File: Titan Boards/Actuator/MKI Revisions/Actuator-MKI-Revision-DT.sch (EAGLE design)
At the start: 104 parts, among them Q1 MOSFET-NCH-AO3404A, Q10 MOSFET-NCH-AO3404A, Q11 MOSFET-NCH-AO3404A, Q12 MOSFET-NCH-AO3404A, Q13 MOSFET-NCH-AO3404A, Q14 MOSFET-NCH-AO3404A, Q15 MOSFET-NCH-AO3404A, Q16 MOSFET-NCH-AO3404A, Q17 MOSFET-NCH-AO3404A, Q18 FDD4141TO252, Q2 MOSFET-NCH-AO3404A, Q3 MOSFET-NCH-AO3404A, Q4 MOSFET-NCH-AO3404A, Q5 MOSFET-NCH-AO3404A, Q6 FDD4141TO252, Q7 MOSFET-NCH-AO3404A, Q8 MOSFET-NCH-AO3404A, Q9 MOSFET-NCH-AO3404A, U1 DRV8816PWPR, U2 W25Q128BVEIG, Y2 16MHz

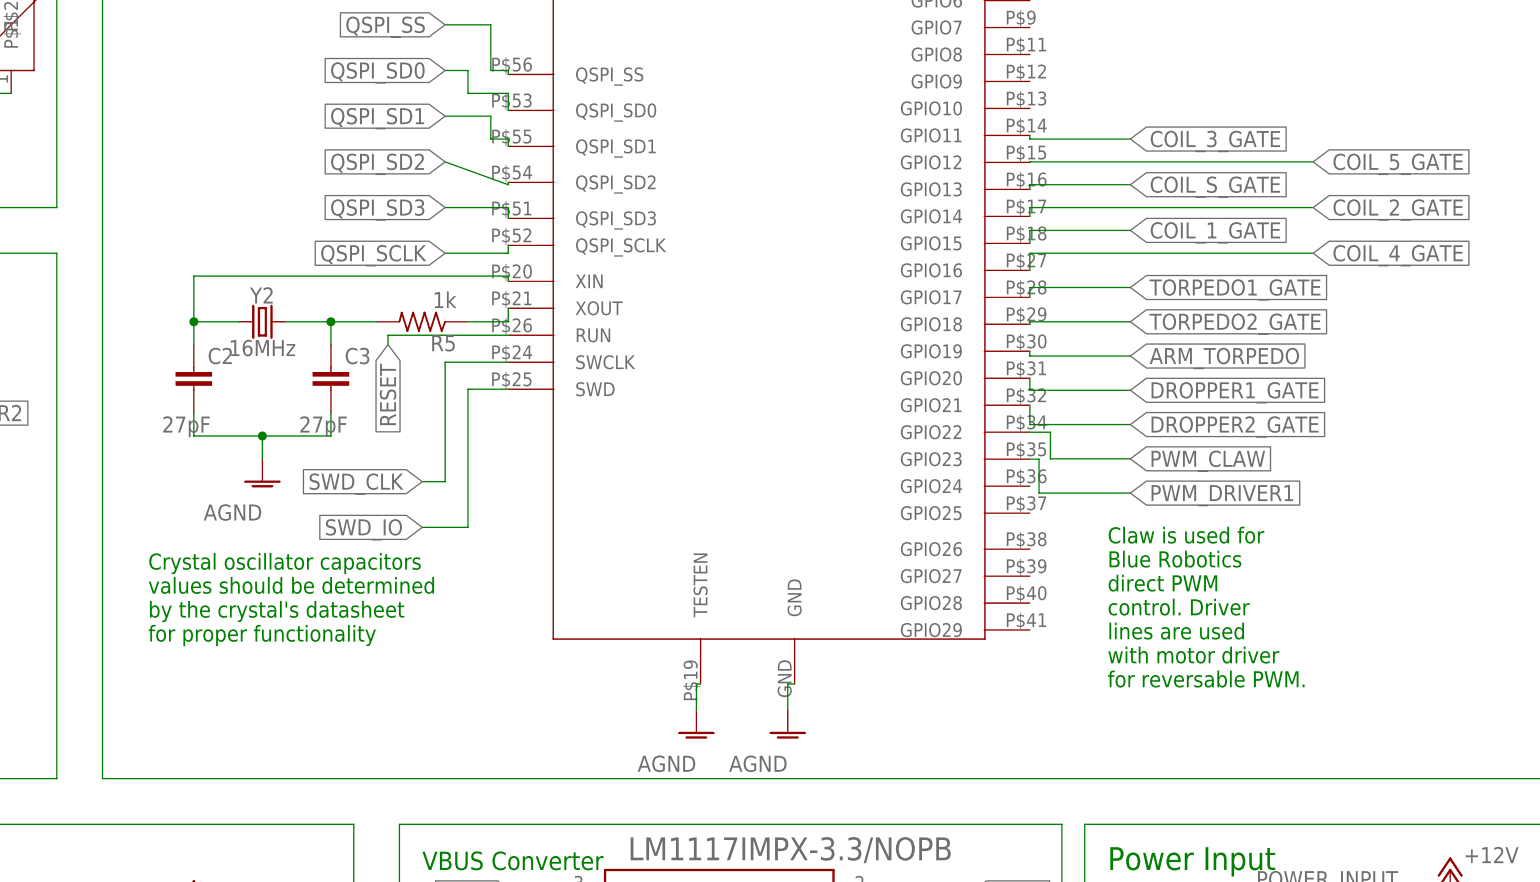
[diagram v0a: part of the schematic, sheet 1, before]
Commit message: Corrected some wiring and moved name tags
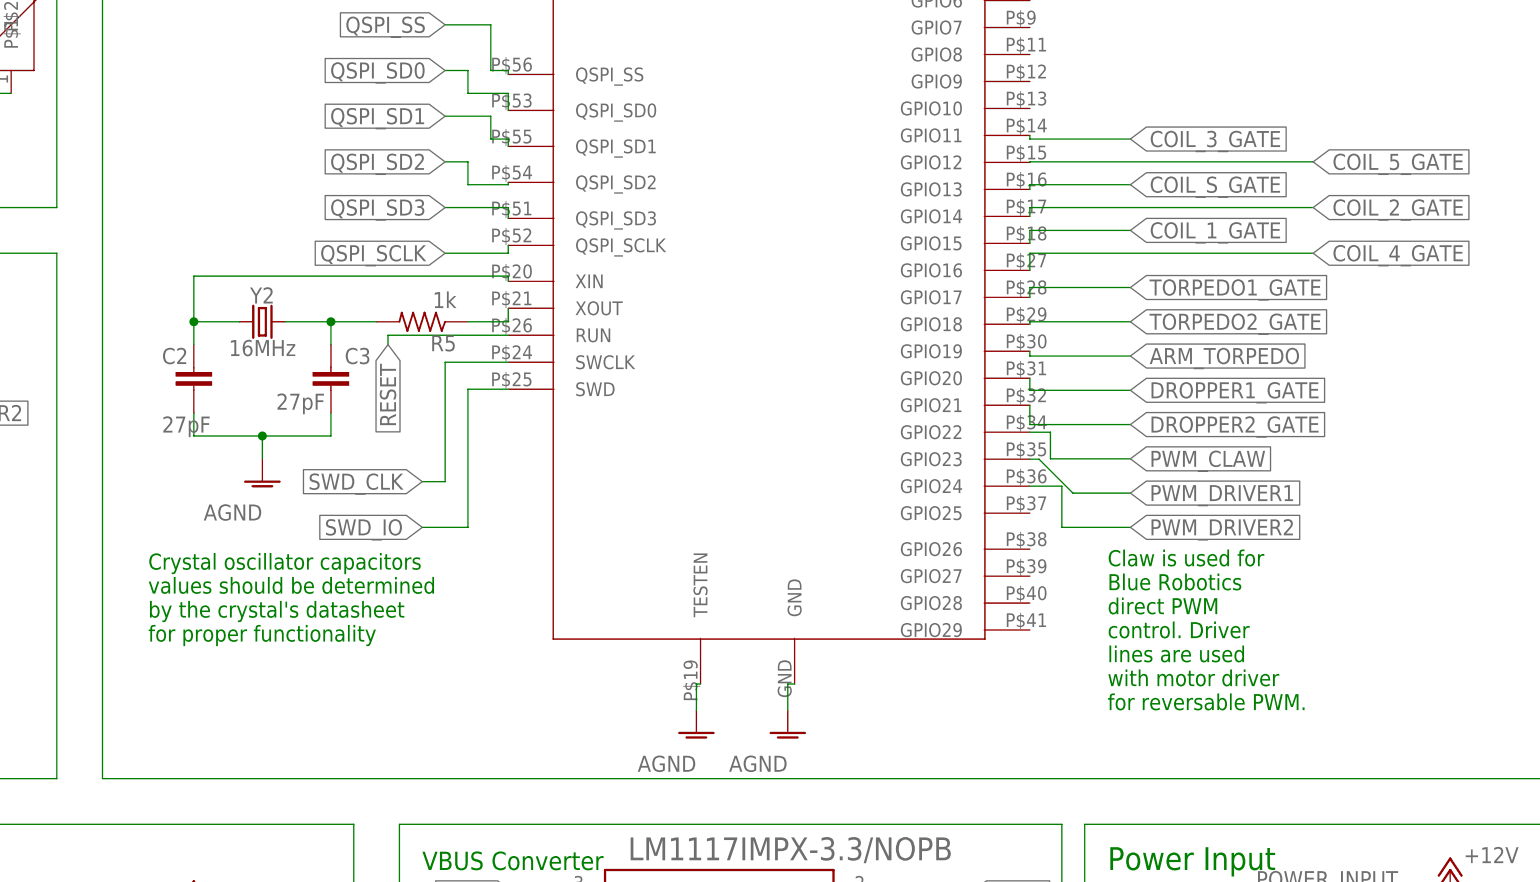
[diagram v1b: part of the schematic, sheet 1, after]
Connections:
- net PWM_DRIVER2: now also U$9.GPIO24
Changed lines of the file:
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@@
 <text x="251.46" y="45.72" size="2.032" layer="91">VBUS Converter</text>
 <text x="274.066" y="246.38" size="2.54" layer="91">PMIC Motor Driver</text>
-<text x="327.66" y="66.04" size="1.778" layer="91">Claw is used for
+<text x="327.66" y="63.5" size="1.778" layer="91">Claw is used for
 Blue Robotics
 direct PWM
@@
 </instance>
 <instance part="C2" gate="G$1" x="226.06" y="101.6" smashed="yes">
-<attribute name="NAME" x="227.584" y="101.981" size="1.778" layer="95"/>
+<attribute name="NAME" x="222.504" y="101.981" size="1.778" layer="95"/>
 <attribute name="VALUE" x="222.504" y="94.361" size="1.778" layer="96"/>
 </instance>
 <instance part="C3" gate="G$1" x="241.3" y="101.6" smashed="yes">
 <attribute name="NAME" x="242.824" y="101.981" size="1.778" layer="95"/>
-<attribute name="VALUE" x="237.744" y="94.361" size="1.778" layer="96"/>
+<attribute name="VALUE" x="235.204" y="96.901" size="1.778" layer="96"/>
 </instance>
 <instance part="AGND3" gate="VR1" x="233.68" y="88.9" smashed="yes">
@@
 <segment>
 <label x="330.2" y="87.63" size="1.778" layer="95" xref="yes"/>
-<wire x1="330.2" y1="87.63" x2="320.04" y2="87.63" width="0.1524" layer="91"/>
-<wire x1="320.04" y1="87.63" x2="320.04" y2="91.4" width="0.1524" layer="91"/>
+<wire x1="330.2" y1="87.63" x2="323.81" y2="87.63" width="0.1524" layer="91"/>
+<wire x1="323.81" y1="87.63" x2="320.04" y2="91.4" width="0.1524" layer="91"/>
 <pinref part="U$9" gate="G$1" pin="GPIO23"/>
 <wire x1="320.04" y1="91.4" x2="319.02" y2="91.4" width="0.1524" layer="91"/>
@@
 <wire x1="285.242" y1="226.06" x2="277.622" y2="226.06" width="0.1524" layer="91"/>
 <label x="277.622" y="226.06" size="1.524" layer="95" rot="R270" xref="yes"/>
+</segment>
+<segment>
+<pinref part="U$9" gate="G$1" pin="GPIO24"/>
+<wire x1="319.02" y1="88.4" x2="322.58" y2="88.4" width="0.1524" layer="91"/>
+<wire x1="322.58" y1="88.4" x2="322.58" y2="83.82" width="0.1524" layer="91"/>
+<wire x1="322.58" y1="83.82" x2="330.2" y2="83.82" width="0.1524" layer="91"/>
+<label x="330.2" y="83.82" size="1.778" layer="95" xref="yes"/>
 </segment>
 </net>
@@
 <pinref part="U$9" gate="G$1" pin="QSPI_SD2"/>
 <wire x1="261.02" y1="122.18" x2="261.02" y2="121.92" width="0.1524" layer="91"/>
-<wire x1="261.02" y1="121.92" x2="254" y2="124.46" width="0.1524" layer="91"/>
+<wire x1="261.02" y1="121.92" x2="256.54" y2="121.92" width="0.1524" layer="91"/>
+<wire x1="256.54" y1="121.92" x2="256.54" y2="124.46" width="0.1524" layer="91"/>
+<wire x1="256.54" y1="124.46" x2="254" y2="124.46" width="0.1524" layer="91"/>
 <label x="254" y="124.46" size="1.778" layer="95" rot="R180" xref="yes"/>
 </segment>

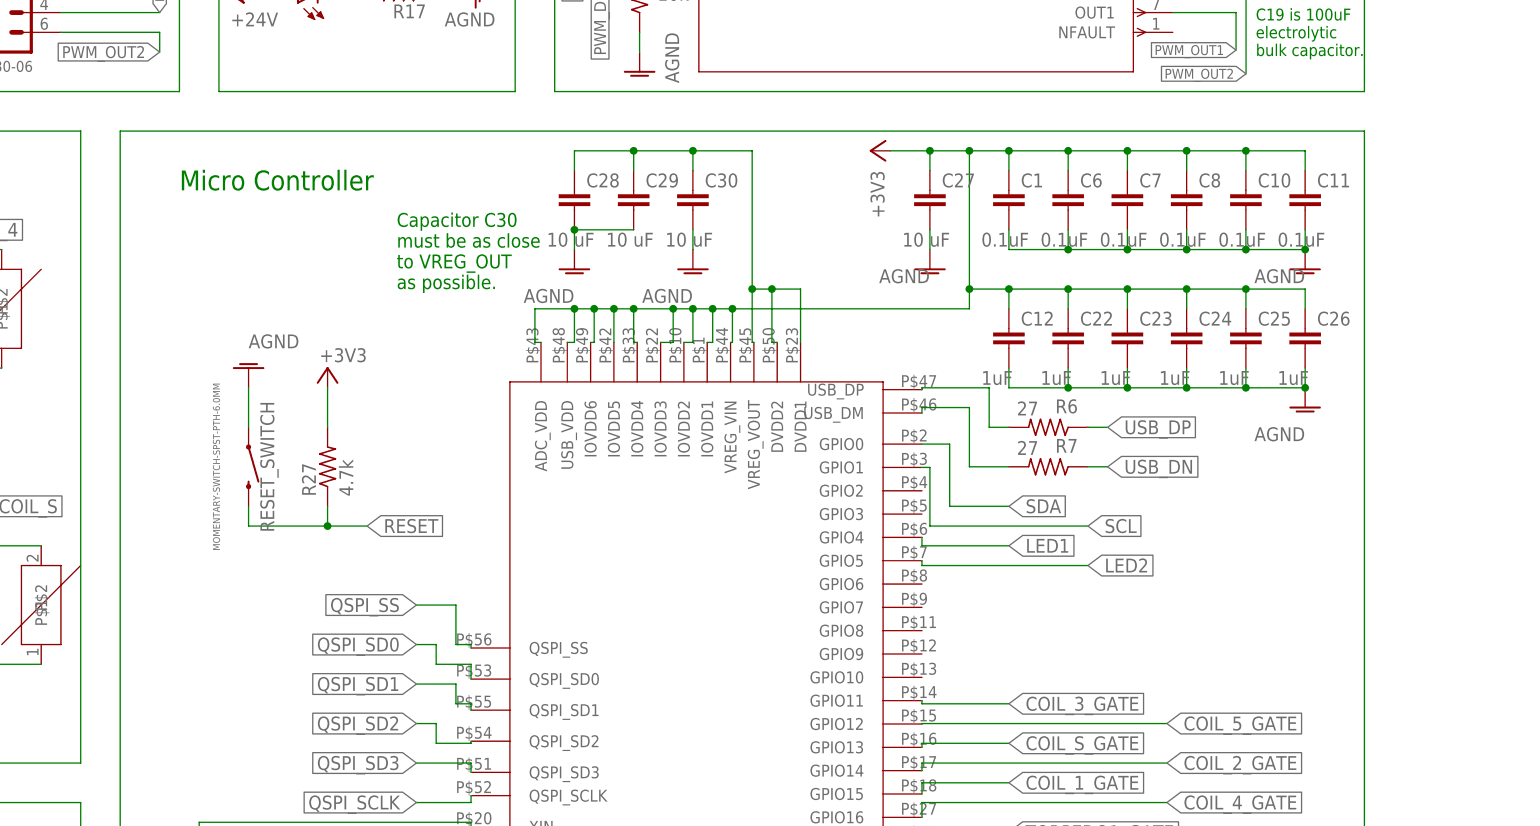
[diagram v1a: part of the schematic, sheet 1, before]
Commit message: start to actuator design review changes
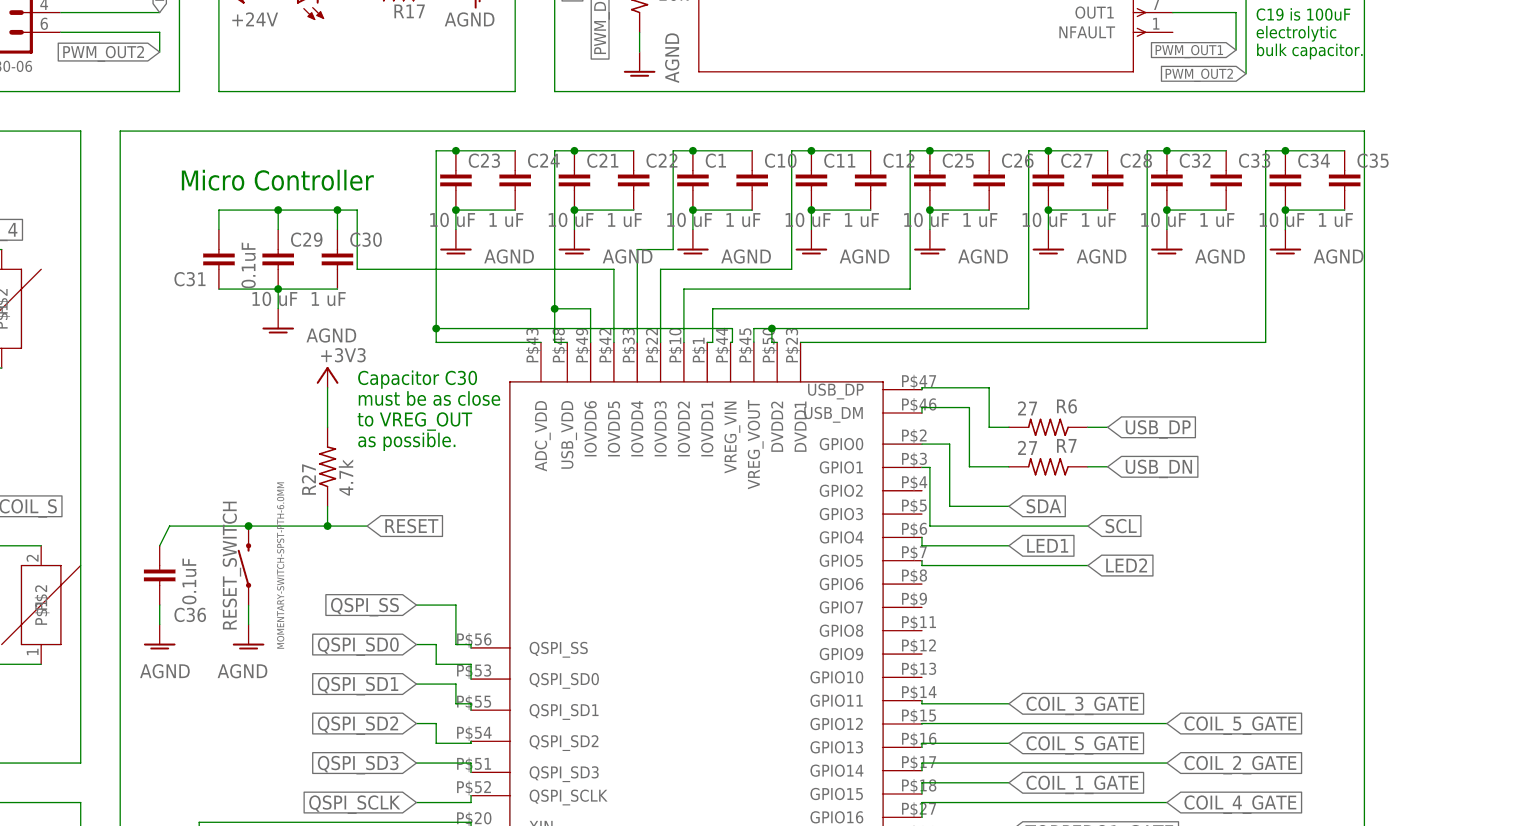
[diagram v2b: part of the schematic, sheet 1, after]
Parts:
- removed C6, C7, C8: 0.1uF, rcl:C-EUC0603
- added C21, C32, C34: 10 uF, rcl:C-EUC0603
- added C31, C36: 0.1uF, rcl:C-EUC0603
- added C33, C35: 1 uF, rcl:C-EUC0603
- C1, C11: value 0.1uF -> 10 uF
- C10: value 0.1uF -> 1 uF
- C12, C22, C24, C26: value 1uF -> 1 uF
- C23, C25: value 1uF -> 10 uF
- C28, C30: value 10 uF -> 1 uF
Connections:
- new net N$24: C11.1, C12.1, U$9.IOVDD3
- new net N$30: C21.1, C22.1, U$9.IOVDD6, U$9.USB_VDD
- new net N$50: C23.1, C24.1, U$9.ADC_VDD, U$9.VREG_VIN
- new net N$51: C27.1, C28.1, U$9.IOVDD1
- new net N$52: C25.1, C26.1, U$9.IOVDD2
- new net N$53: C32.1, C33.1, U$9.DVDD2, U$9.VREG_VOUT
- new net N$54: C34.1, C35.1, U$9.DVDD1
- new net N$55: C29.1, C30.1, C31.2, U$9.IOVDD5
- net +3V3: no longer C1.1, C10.1, C11.1, C12.1, C22.1, C23.1, C24.1, C25.1, C26.1, C27.1, C6.1, C7.1, C8.1, U$9.ADC_VDD, U$9.IOVDD1, U$9.IOVDD2, U$9.IOVDD3, U$9.IOVDD4, U$9.IOVDD5, U$9.IOVDD6, U$9.USB_VDD, U$9.VREG_VIN
- net AGND: now also C21.2, C31.1, C32.2, C33.2, C34.2, C35.2, C36.1; no longer C6.2, C7.2, C8.2
- net N$5: now also C1.1, C10.1, U$9.IOVDD4; no longer C28.1, C29.1, C30.1, U$9.DVDD1, U$9.DVDD2, U$9.VREG_VOUT
- net RESET: now also C36.2
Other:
- moved on the sheet: C1, C10, C11, C12, C22, C23, C24, C25, C26, C27, C28, C29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

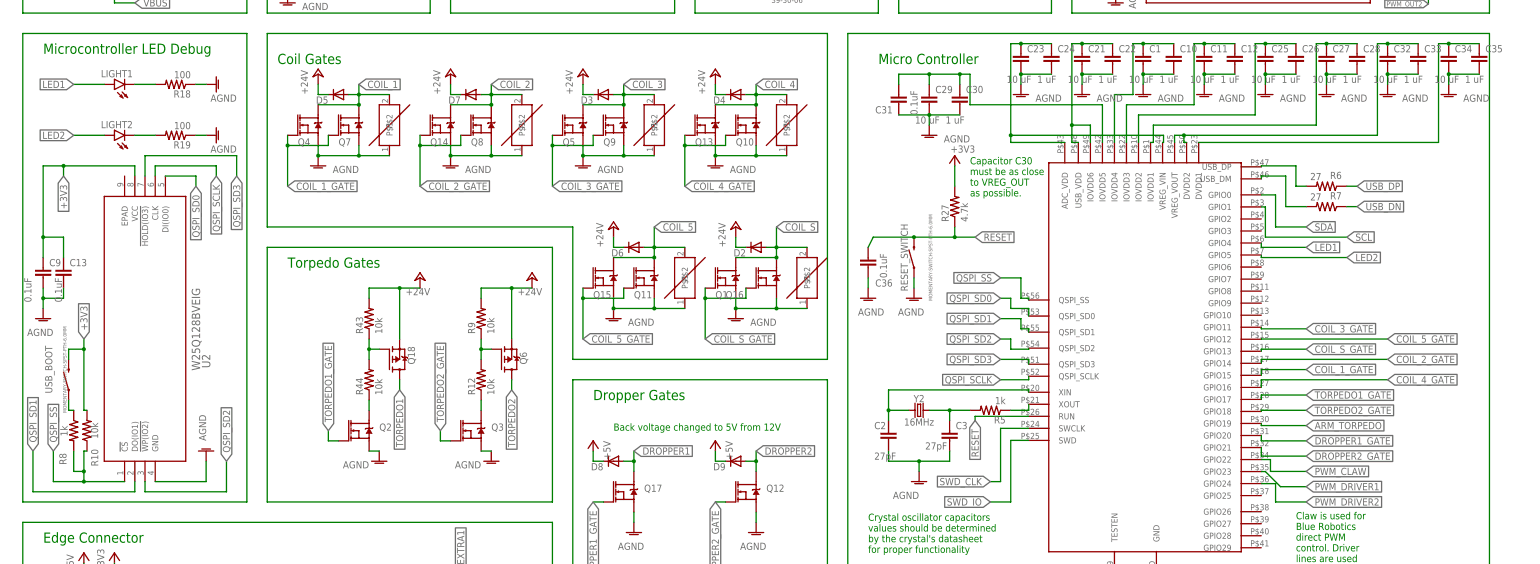
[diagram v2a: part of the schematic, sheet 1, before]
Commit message: Adjusted wires for design rules
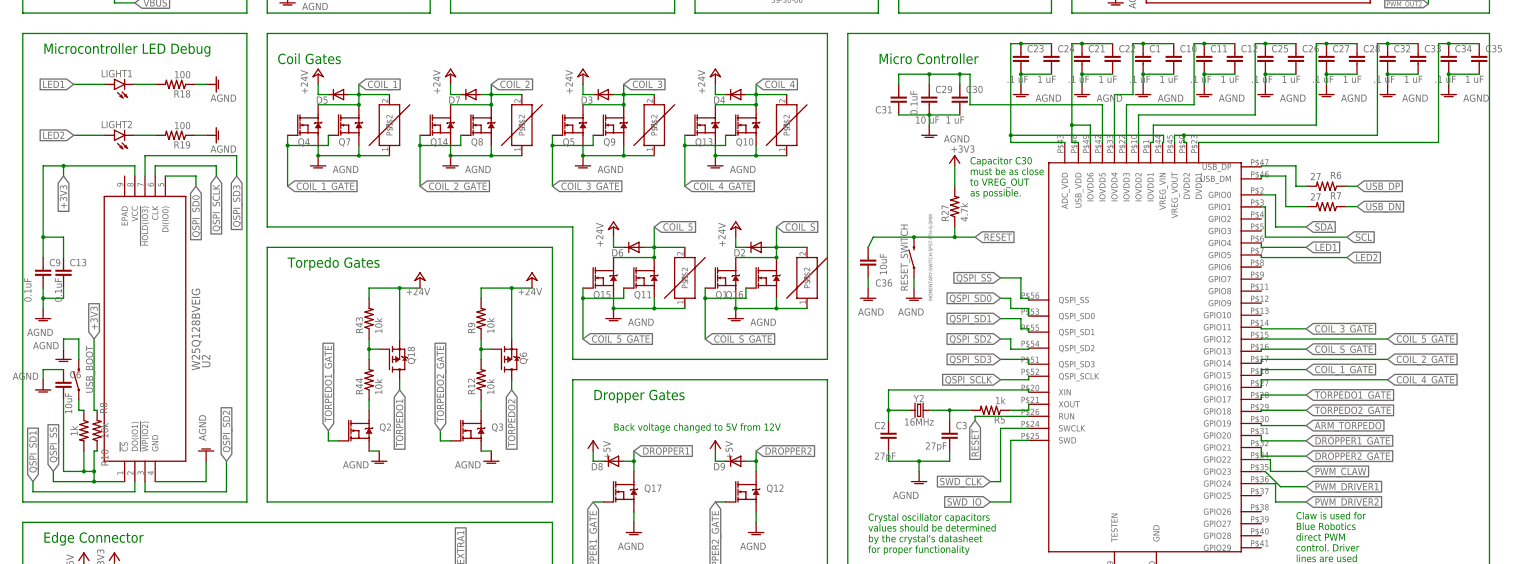
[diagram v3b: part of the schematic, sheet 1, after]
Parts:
- added C6: 10uF, rcl:C-EUC0603
- C1, C11, C21, C23, C25, C27, C32, C34: value 10 uF -> .1 uF
- C36: value 0.1uF -> 10uF
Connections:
- net +3V3: no longer USB_BOOT.2
- net AGND: now also C6.1, USB_BOOT.2
- net QSPI_SS: now also C6.2
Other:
- moved on the sheet: R10, R8, USB_BOOT

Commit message: Actuator work
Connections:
- removed net N$24: C11.1, C12.1, U$9.IOVDD3
- removed net N$30: C21.1, C22.1, U$9.IOVDD6, U$9.USB_VDD
- removed net N$5: C1.1, C10.1, U$9.IOVDD4
- removed net N$50: C23.1, C24.1, U$9.ADC_VDD, U$9.VREG_VIN
- removed net N$51: C27.1, C28.1, U$9.IOVDD1
- removed net N$52: C25.1, C26.1, U$9.IOVDD2
- removed net N$53: C32.1, C33.1, U$9.DVDD2, U$9.VREG_VOUT
- removed net N$54: C34.1, C35.1, U$9.DVDD1
- removed net N$55: C29.1, C30.1, C31.2, U$9.IOVDD5
- net +3V3: now also C1.1, C10.1, C11.1, C12.1, C21.1, C22.1, C23.1, C24.1, C25.1, C26.1, C27.1, C28.1, C29.1, C30.1, C31.2, C32.1, C33.1, C34.1, C35.1, U$9.ADC_VDD, U$9.DVDD1, U$9.DVDD2, U$9.IOVDD1, U$9.IOVDD2, U$9.IOVDD3, U$9.IOVDD4, U$9.IOVDD5, U$9.IOVDD6, U$9.USB_VDD, U$9.VREG_VIN, U$9.VREG_VOUT
